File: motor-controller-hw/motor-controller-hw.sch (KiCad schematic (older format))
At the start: 31 parts, among them J101 CAN, J102 Throttle, J103 Motor Temp, J104 Transistor Temp, J105 USB_B_Micro, J106 Extra IO, J107 Hall Sensors, J108 CAN_DBG, J109 ABN Encoder, J110 SPI_DBG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

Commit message: Finished adding footprints to the schematic, started layout
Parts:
- C103: footprint (none) -> Capacitor_THT:CP_Radial_D8.0mm_P3.50mm
- D101, D102: footprint (none) -> Diode_SMD:D_SOD-123F
- F101, F102, F103: footprint (none) -> Fuse:Fuse_0603_1608Metric_Pad1.05x0.95mm_HandSolder
- J103, J104: footprint (none) -> supermileage_footprints:Molex-duraClick-2conn
- J105: footprint (none) -> supermileage_footprints:USB_Micro-B
- J106: footprint (none) -> supermileage_footprints:Molex-UltraFit-14p-vert
- J107: footprint (none) -> supermileage_footprints:MICRO_JST_6
- Q101: footprint (none) -> Package_TO_SOT_SMD:TO-252-3_TabPin2
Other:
- note added: "5V switching regulator, up to 50V input, maximum 600mA output current. \nThe regulator is short circuit protected.\nA P-Channel MOSFET is used as an ideal diode with a 18v zener diode to\nprotect the MOSFET gate. The 10K resistor limits the zener diode current\nto 3mA at 48V input. A Schotty diode is used to protect the USB 5V line\nfrom reverse current."
- note removed: "5V switching regulator, up to 50V input, maximum 600mA output current. \nThe regulator is short circuit protected.\nA P-Channel MOSFET is used as an ideal diode with a 18v zener diode to\nprotect the MOSFET gate. The 10K resistor limits the zener diode current\nto 3mA at 48V input. A Shocktty diode is used to protect the USB 5V line\nfrom reverse current."
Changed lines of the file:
@@
 F 0 "C103" H 3400 2150 50  0000 L CNN
 F 1 "33u" H 3400 1950 50  0000 L CNN
-F 2 "" H 3388 1900 50  0001 C CNN
+F 2 "Capacitor_THT:CP_Radial_D8.0mm_P3.50mm" H 3388 1900 50  0001 C CNN
 F 3 "" H 3350 2050 50  0001 C CNN
 	1    3350 2050
@@
 3.3V linear voltage regulator for the low voltage electronics. The selected\nregulator can supply 1A of output current, which is more than what the 5V \nswitching regulator can supply. The 4.7uF output capacitor should have a \nfairly low ESR.
 Text Notes 1850 1050 0    50   ~ 0
-5V switching regulator, up to 50V input, maximum 600mA output current. \nThe regulator is short circuit protected.\nA P-Channel MOSFET is used as an ideal diode with a 18v zener diode to\nprotect the MOSFET gate. The 10K resistor limits the zener diode current\nto 3mA at 48V input. A Shocktty diode is used to protect the USB 5V line\nfrom reverse current.
+5V switching regulator, up to 50V input, maximum 600mA output current. \nThe regulator is short circuit protected.\nA P-Channel MOSFET is used as an ideal diode with a 18v zener diode to\nprotect the MOSFET gate. The 10K resistor limits the zener diode current\nto 3mA at 48V input. A Schotty diode is used to protect the USB 5V line\nfrom reverse current.
 $Comp
 L Device:Q_PMOS_GDS Q101
@@
 F 0 "Q101" V 2700 1850 50  0000 C CNN
 F 1 "Q_PMOS_GDS" V 2300 2150 50  0000 C CNN
-F 2 "" H 2650 1950 50  0001 C CNN
+F 2 "Package_TO_SOT_SMD:TO-252-3_TabPin2" H 2650 1950 50  0001 C CNN
 F 3 "~" H 2450 1850 50  0001 C CNN
 	1    2450 1850
@@
 F 0 "D101" V 2950 2000 50  0000 L CNN
 F 1 "18V Zener" H 2700 1850 50  0000 L CNN
-F 2 "" H 2850 1950 50  0001 C CNN
+F 2 "Diode_SMD:D_SOD-123F" H 2850 1950 50  0001 C CNN
 F 3 "~" H 2850 1950 50  0001 C CNN
 	1    2850 1950
@@
 F 0 "J105" H 1050 800 50  0000 C CNN
 F 1 "USB_B_Micro" H 900 1550 50  0000 C CNN
-F 2 "" H 1050 1150 50  0001 C CNN
+F 2 "supermileage_footprints:USB_Micro-B" H 1050 1150 50  0001 C CNN
 F 3 "~" H 1050 1150 50  0001 C CNN
 	1    900  1200
@@
 F 0 "J103" H 800 4450 50  0000 C CNN
 F 1 "Motor Temp" H 800 4050 50  0000 C CNN
-F 2 "" H 800 4300 50  0001 C CNN
+F 2 "supermileage_footprints:Molex-duraClick-2conn" H 800 4300 50  0001 C CNN
 F 3 "~" H 800 4300 50  0001 C CNN
 	1    800  4300
@@
 F 0 "J104" H 800 5300 50  0000 C CNN
 F 1 "Transistor Temp" H 720 4916 50  0000 C CNN
-F 2 "" H 800 5150 50  0001 C CNN
+F 2 "supermileage_footprints:Molex-duraClick-2conn" H 800 5150 50  0001 C CNN
 F 3 "~" H 800 5150 50  0001 C CNN
 	1    800  5150
@@
 F 0 "J106" H 1450 5750 50  0000 C CNN
 F 1 "Extra IO" H 1450 6626 50  0000 C CNN
-F 2 "" H 1400 6200 50  0001 C CNN
+F 2 "supermileage_footprints:Molex-UltraFit-14p-vert" H 1400 6200 50  0001 C CNN
 F 3 "~" H 1400 6200 50  0001 C CNN
 	1    1400 6200
@@
 F 0 "F101" V 1250 3300 50  0000 C CNN
 F 1 "50mA PTC" V 1150 3300 50  0000 C CNN
-F 2 "" H 1400 3150 50  0001 L CNN
+F 2 "Fuse:Fuse_0603_1608Metric_Pad1.05x0.95mm_HandSolder" H 1400 3150 50  0001 L CNN
 F 3 "~" H 1350 3350 50  0001 C CNN
 	1    1350 3350
@@
 F 0 "J107" H 2000 5300 50  0000 C CNN
 F 1 "Hall Sensors" V 2100 4900 50  0000 C CNN
-F 2 "" H 2000 4950 50  0001 C CNN
+F 2 "supermileage_footprints:MICRO_JST_6" H 2000 4950 50  0001 C CNN
 F 3 "~" H 2000 4950 50  0001 C CNN
 	1    2000 4950
@@
 F 0 "D102" H 2950 1550 50  0000 C CNN
 F 1 "D_USB" H 2950 1350 50  0000 C CNN
-F 2 "" H 2950 1450 50  0001 C CNN
+F 2 "Diode_SMD:D_SOD-123F" H 2950 1450 50  0001 C CNN
 F 3 "~" H 2950 1450 50  0001 C CNN
 	1    2950 1450
@@
 F 0 "F103" V 1900 5800 50  0000 C CNN
 F 1 "50mA PTC" V 1800 5950 50  0001 C CNN
-F 2 "" H 1900 5800 50  0001 L CNN
+F 2 "Fuse:Fuse_0603_1608Metric_Pad1.05x0.95mm_HandSolder" H 1900 5800 50  0001 L CNN
 F 3 "~" H 1850 6000 50  0001 C CNN
 	1    1850 6000
@@
 F 0 "F102" V 1900 5700 50  0000 C CNN
 F 1 "50mA PTC" V 2000 5850 50  0000 C CNN
-F 2 "" H 1900 5700 50  0001 L CNN
+F 2 "Fuse:Fuse_0603_1608Metric_Pad1.05x0.95mm_HandSolder" H 1900 5700 50  0001 L CNN
 F 3 "~" H 1850 5900 50  0001 C CNN
 	1    1850 5900

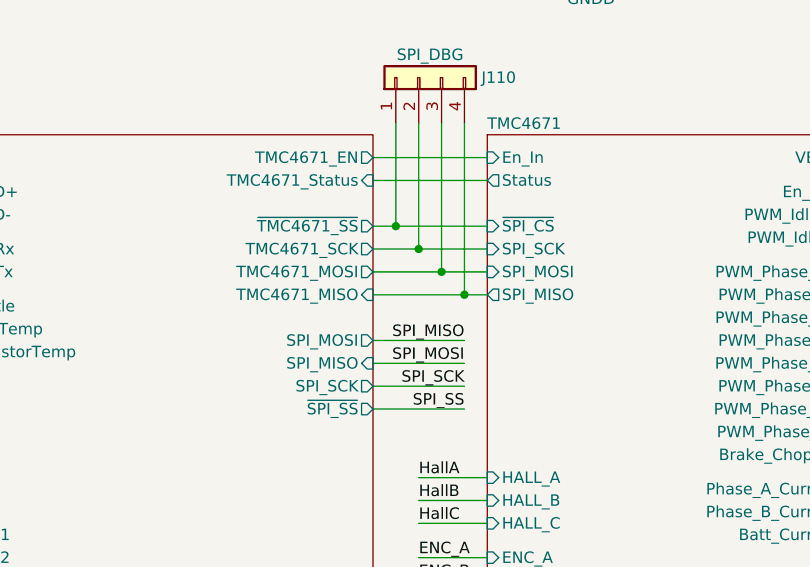
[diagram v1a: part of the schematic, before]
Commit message: Moved chaged order of op-amps to make PCB layout easier. More pcb part positioning
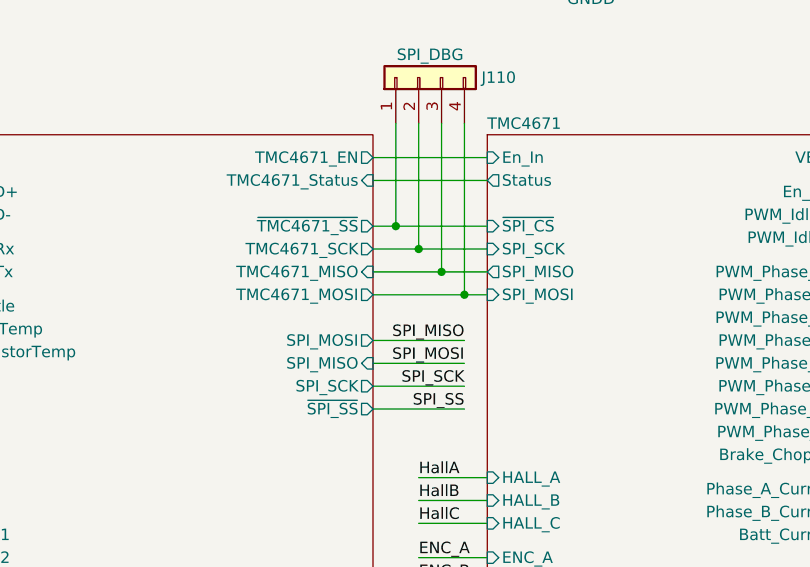
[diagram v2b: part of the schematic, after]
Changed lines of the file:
@@
 F21 "~TMC4671_SS" O R 7650 4450 50
 F22 "TMC4671_SCK" O R 7650 4550 50
-F23 "TMC4671_MISO" I R 7650 4750 50
-F24 "TMC4671_MOSI" O R 7650 4650 50
+F23 "TMC4671_MISO" I R 7650 4650 50
+F24 "TMC4671_MOSI" O R 7650 4750 50
 F25 "TMC4671_EN" O R 7650 4150 50
 F26 "TMC4671_Status" I R 7650 4250 50
@@
 F8 "~SPI_CS" I L 8150 4450 50
 F9 "SPI_SCK" I L 8150 4550 50
-F10 "SPI_MOSI" I L 8150 4650 50
-F11 "SPI_MISO" O L 8150 4750 50
+F10 "SPI_MOSI" I L 8150 4750 50
+F11 "SPI_MISO" O L 8150 4650 50
 F12 "HALL_A" I L 8150 5550 50
 F13 "HALL_B" I L 8150 5650 50

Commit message: Adding BOM, changed some footprints -Changed footprints to linux models in schematics -Added field Digi-key# to all components -Started filling in said field
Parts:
- added D103: Vin, LEDs:LED_0603_HandSoldering, symbol MotorControllerParts:LED_ALT
- added D104: 5V, LEDs:LED_0603_HandSoldering, symbol MotorControllerParts:LED_ALT
- added D105: 3.3V, LEDs:LED_0603_HandSoldering, symbol MotorControllerParts:LED_ALT
- added R103: 10K, Resistors_SMD:R_0805_HandSoldering, symbol MotorControllerParts:R
- added R104: 1K, Resistors_SMD:R_0805_HandSoldering, symbol MotorControllerParts:R
- added R105: 510R, Resistors_SMD:R_0805_HandSoldering, symbol MotorControllerParts:R
- C101, C104: footprint Capacitor_SMD:C_0805_2012Metric_Pad1.15x1.40mm_HandSolder -> Capacitors_SMD:C_0805_HandSoldering; Digi-key# (none) -> 732-7628-1-ND
- C102: footprint Capacitor_SMD:C_0805_2012Metric_Pad1.15x1.40mm_HandSolder -> Capacitors_SMD:C_0805_HandSoldering; Digi-key# (none) -> 1276-2444-1-ND
- C103: Digi-key# (none) -> P10340-ND
- C105: value 10u -> 4u7; footprint Capacitor_SMD:C_0805_2012Metric_Pad1.15x1.40mm_HandSolder -> Capacitors_SMD:C_0805_HandSoldering; Digi-key# (none) -> 732-7628-1-ND
- D101: value 18V Zener -> 15V Zener; Digi-key# (none) -> BZT52HC15WF-7DICT-ND‎
- D102: Digi-key# (none) -> MBR1020VLCT-ND‎
- F101, F102, F103: Digi-key# (none) -> 507-1816-1-ND
- J101, J102: Digi-key# (none) -> WM7171CT-ND
- J103: value Motor Temp -> Motor T; Digi-key# (none) -> WM7169CT-ND
- J104: value Transistor Temp -> Tran T; Digi-key# (none) -> WM7169CT-ND
- J105: Digi-key# (none) -> 609-4618-1-ND
- J106: Digi-key# (none) -> WM11743-ND‎
- J107: Digi-key# (none) -> 455-1708-ND
- Q101: Digi-key# (none) -> 785-1102-1-ND
- R101, R102: footprint Resistor_SMD:R_0805_2012Metric_Pad1.15x1.40mm_HandSolder -> Resistors_SMD:R_0805_HandSoldering
- TP101: value 5v_TP -> Batt_TP; Digi-key# (none) -> N/A
- TP102, TP103, TP104, TP105: Digi-key# (none) -> N/A
- U101: Digi-key# (none) -> AP7361C-33E-13DICT-ND
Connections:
- wire segments 245 -> 260
- no-connect marks 14 -> 21
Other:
- note added: "Power Status LEDs"

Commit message: Moved some parts into the project parts library messed with the PCB slightly
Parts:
- D101: symbol Device:D_Zener_ALT -> MotorControllerParts:D_Zener_ALT
- Q101: symbol Device:Q_PMOS_GDS -> MotorControllerParts:Q_PMOS_GDS
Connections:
- no-connect marks 21 -> 22
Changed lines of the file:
@@
 	3600 6950 3700 6950
 $Comp
-L power:+5V #PWR0111
+L MotorControllerParts:+5V #PWR0111
 U 1 1 5BBE81EF
 P 3550 3850
@@
 5V switching regulator, up to 50V input, maximum 600mA output current. \nThe regulator is short circuit protected.\nA P-Channel MOSFET is used as an ideal diode with a 18v zener diode to\nprotect the MOSFET gate. The 10K resistor limits the zener diode current\nto 3mA at 48V input. A Schotty diode is used to protect the USB 5V line\nfrom reverse current.
 $Comp
-L Device:Q_PMOS_GDS Q101
+L MotorControllerParts:Q_PMOS_GDS Q101
 U 1 1 5BFA3DE2
 P 2450 1850
@@
 $EndComp
 $Comp
-L Device:D_Zener_ALT D101
+L MotorControllerParts:D_Zener_ALT D101
 U 1 1 5BFA3DE9
 P 2850 1950
@@
 Throttle
 $Comp
-L power:+5V #PWR0107
+L MotorControllerParts:+5V #PWR0107
 U 1 1 5C00DC4D
 P 1550 3150
@@
 $EndComp
 $Comp
-L power:+5V #PWR0108
+L MotorControllerParts:+5V #PWR0108
 U 1 1 5C06D333
 P 2200 5850
@@
 $EndComp
 $Comp
-L power:+5V #PWR0113
+L MotorControllerParts:+5V #PWR0113
 U 1 1 5BF8E00C
 P 2300 4350
@@
 P 2650 4350
 F 0 "#PWR0115" H 2650 4200 50  0001 C CNN
-F 1 "+3.3V" H 2600 4550 50  0000 C CNN
+F 1 "+3.3V" H 2650 4550 50  0000 C CNN
 F 2 "" H 2650 4350 50  0001 C CNN
 F 3 "" H 2650 4350 50  0001 C CNN
@@
 $EndComp
 $Comp
-L power:+5V #PWR0118
+L MotorControllerParts:+5V #PWR0118
 U 1 1 5E78636F
 P 2400 3250
@@
 ENC_A_in
 $Comp
-L power:+5V #PWR0140
+L MotorControllerParts:+5V #PWR0140
 U 1 1 5E8886B9
 P 10150 900
@@
 	7000 2700 7100 2700
 $Comp
-L power:+5V #PWR0143
+L MotorControllerParts:+5V #PWR0143
 U 1 1 5C172733
 P 6100 2650
@@
 Text Notes 6150 2400 0    50   ~ 0
 Power Status LEDs
+NoConn ~ 9900 1750
 $EndSCHEMATC

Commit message: Added all of the digi-key part numbers
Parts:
- D103, D104, D105: Digi-key# (none) -> 732-12015-1-ND
- J108: Digi-key# (none) -> S1212EC-02-ND
- J109: Digi-key# (none) -> S1212EC-05-ND
- J110: Digi-key# (none) -> S1212EC-04-ND
- J111: Digi-key# (none) -> S7125-ND
- R101, R102, R103: Digi-key# (none) -> A129761CT-ND
- R104: Digi-key# (none) -> A129749CT-ND
- R105: value 510R -> 330R; Digi-key# (none) -> 311-330CRCT-ND
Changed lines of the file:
@@
 F 1 "10K" H 2450 4550 50  0000 L CNN
 F 2 "Resistors_SMD:R_0805_HandSoldering" V 2580 4550 50  0001 C CNN
-F 3 "" H 2650 4550 50  0001 C CNN
+F 3 "https://www.te.com/commerce/DocumentDelivery/DDEController?Action=srchrtrv&DocNm=1773204-3&DocType=DS&DocLang=English" H 2650 4550 50  0001 C CNN
+F 4 "A129761CT-ND" H 0   0   50  0001 C CNN "Digi-key#"
 	1    2650 4550
 	1    0    0    -1
@@
 F 1 "Trinamic-Bridge" H 9275 924 50  0000 C CNN
 F 2 "Connector_PinSocket_2.54mm:PinSocket_2x22_P2.54mm_Vertical" H 8750 2150 50  0001 C CNN
-F 3 "" H 8750 2150 50  0001 C CNN
+F 3 "https://drawings-pdf.s3.amazonaws.com/10492.pdf" H 8750 2150 50  0001 C CNN
+F 4 "S7125-ND" H 0   0   50  0001 C CNN "Digi-key#"
 	1    9250 2150
 	1    0    0    1
@@
 F 1 "10K" H 2200 2300 50  0000 L CNN
 F 2 "Resistors_SMD:R_0805_HandSoldering" V 2380 2350 50  0001 C CNN
-F 3 "~" H 2450 2350 50  0001 C CNN
+F 3 "https://www.te.com/commerce/DocumentDelivery/DDEController?Action=srchrtrv&DocNm=1773204-3&DocType=DS&DocLang=English" H 2450 2350 50  0001 C CNN
+F 4 "A129761CT-ND" H 0   0   50  0001 C CNN "Digi-key#"
 	1    2450 2350
 	-1   0    0    -1
@@
 F 1 "CAN_DBG" V 5300 3750 50  0000 C CNN
 F 2 "Connector_PinHeader_2.54mm:PinHeader_1x02_P2.54mm_Vertical" H 5200 3800 50  0001 C CNN
-F 3 "~" H 5200 3800 50  0001 C CNN
+F 3 "https://media.digikey.com/PDF/Data%20Sheets/Sullins%20PDFs/xRxCzzzSxxN-RC_ST_11635-B.pdf" H 5200 3800 50  0001 C CNN
+F 4 "S1212EC-02-ND" H 0   0   50  0001 C CNN "Digi-key#"
 	1    5200 3800
 	0    -1   -1   0
@@
 F 1 "SPI_DBG" V 7950 3750 50  0000 C CNN
 F 2 "Connector_PinHeader_2.54mm:PinHeader_1x04_P2.54mm_Vertical" H 7850 3800 50  0001 C CNN
-F 3 "~" H 7850 3800 50  0001 C CNN
+F 3 "https://media.digikey.com/PDF/Data%20Sheets/Sullins%20PDFs/xRxCzzzSxxN-RC_ST_11635-B.pdf" H 7850 3800 50  0001 C CNN
+F 4 "S1212EC-04-ND" H 0   0   50  0001 C CNN "Digi-key#"
 	1    7850 3800
 	0    -1   -1   0
@@
 F 1 "ABN Encoder" V 2200 3550 50  0000 C CNN
 F 2 "Connector_PinHeader_2.54mm:PinHeader_1x05_P2.54mm_Vertical" H 2100 3550 50  0001 C CNN
-F 3 "~" H 2100 3550 50  0001 C CNN
+F 3 "https://media.digikey.com/PDF/Data%20Sheets/Sullins%20PDFs/xRxCzzzSxxN-RC_ST_11635-B.pdf" H 2100 3550 50  0001 C CNN
+F 4 "S1212EC-05-ND" H 0   0   50  0001 C CNN "Digi-key#"
 	1    2100 3550
 	-1   0    0    1
@@
 F 1 "Vin" H 5792 2536 50  0000 C CNN
 F 2 "LEDs:LED_0603_HandSoldering" H 5800 2700 50  0001 C CNN
-F 3 "~" H 5800 2700 50  0001 C CNN
+F 3 "https://katalog.we-online.de/pbs/datasheet/150060RS55040.pdf" H 5800 2700 50  0001 C CNN
+F 4 "732-12015-1-ND" H 0   0   50  0001 C CNN "Digi-key#"
 	1    5800 2700
 	-1   0    0    1
@@
 F 1 "5V" H 6692 2536 50  0000 C CNN
 F 2 "LEDs:LED_0603_HandSoldering" H 6700 2700 50  0001 C CNN
-F 3 "~" H 6700 2700 50  0001 C CNN
+F 3 "https://katalog.we-online.de/pbs/datasheet/150060RS55040.pdf" H 6700 2700 50  0001 C CNN
+F 4 "732-12015-1-ND" H 0   0   50  0001 C CNN "Digi-key#"
 	1    6700 2700
 	-1   0    0    1
@@
 F 1 "3.3V" H 7592 2536 50  0000 C CNN
 F 2 "LEDs:LED_0603_HandSoldering" H 7600 2700 50  0001 C CNN
-F 3 "~" H 7600 2700 50  0001 C CNN
+F 3 "https://katalog.we-online.de/pbs/datasheet/150060RS55040.pdf" H 7600 2700 50  0001 C CNN
+F 4 "732-12015-1-ND" H 0   0   50  0001 C CNN "Digi-key#"
 	1    7600 2700
 	-1   0    0    1
@@
 P 7250 2700
 F 0 "R105" V 7350 2700 50  0000 C CNN
-F 1 "510R" V 7134 2700 50  0000 C CNN
+F 1 "330R" V 7134 2700 50  0000 C CNN
 F 2 "Resistors_SMD:R_0805_HandSoldering" V 7180 2700 50  0001 C CNN
-F 3 "~" H 7250 2700 50  0001 C CNN
+F 3 "http://www.yageo.com/documents/recent/PYu-RC_Group_51_RoHS_L_9.pdf" H 7250 2700 50  0001 C CNN
+F 4 "311-330CRCT-ND" H 0   0   50  0001 C CNN "Digi-key#"
 	1    7250 2700
 	0    1    1    0
@@
 F 1 "1K" V 6234 2700 50  0000 C CNN
 F 2 "Resistors_SMD:R_0805_HandSoldering" V 6280 2700 50  0001 C CNN
-F 3 "~" H 6350 2700 50  0001 C CNN
+F 3 "https://www.te.com/commerce/DocumentDelivery/DDEController?Action=srchrtrv&DocNm=1773204-3&DocType=DS&DocLang=English" H 6350 2700 50  0001 C CNN
+F 4 "A129749CT-ND" H 0   0   50  0001 C CNN "Digi-key#"
 	1    6350 2700
 	0    1    1    0
@@
 F 1 "10K" V 5334 2700 50  0000 C CNN
 F 2 "Resistors_SMD:R_0805_HandSoldering" V 5380 2700 50  0001 C CNN
-F 3 "~" H 5450 2700 50  0001 C CNN
+F 3 "https://www.te.com/commerce/DocumentDelivery/DDEController?Action=srchrtrv&DocNm=1773204-3&DocType=DS&DocLang=English" H 5450 2700 50  0001 C CNN
+F 4 "A129761CT-ND" H 0   0   50  0001 C CNN "Digi-key#"
 	1    5450 2700
 	0    1    1    0
